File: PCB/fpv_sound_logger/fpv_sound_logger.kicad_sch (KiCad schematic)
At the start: 26 parts, among them IC1 W25Q128JVSIQ, IC2 NCP1117ST33T3G, J1 DM3D-SF, U1 RP2040, Y1 ABM8-272-T3

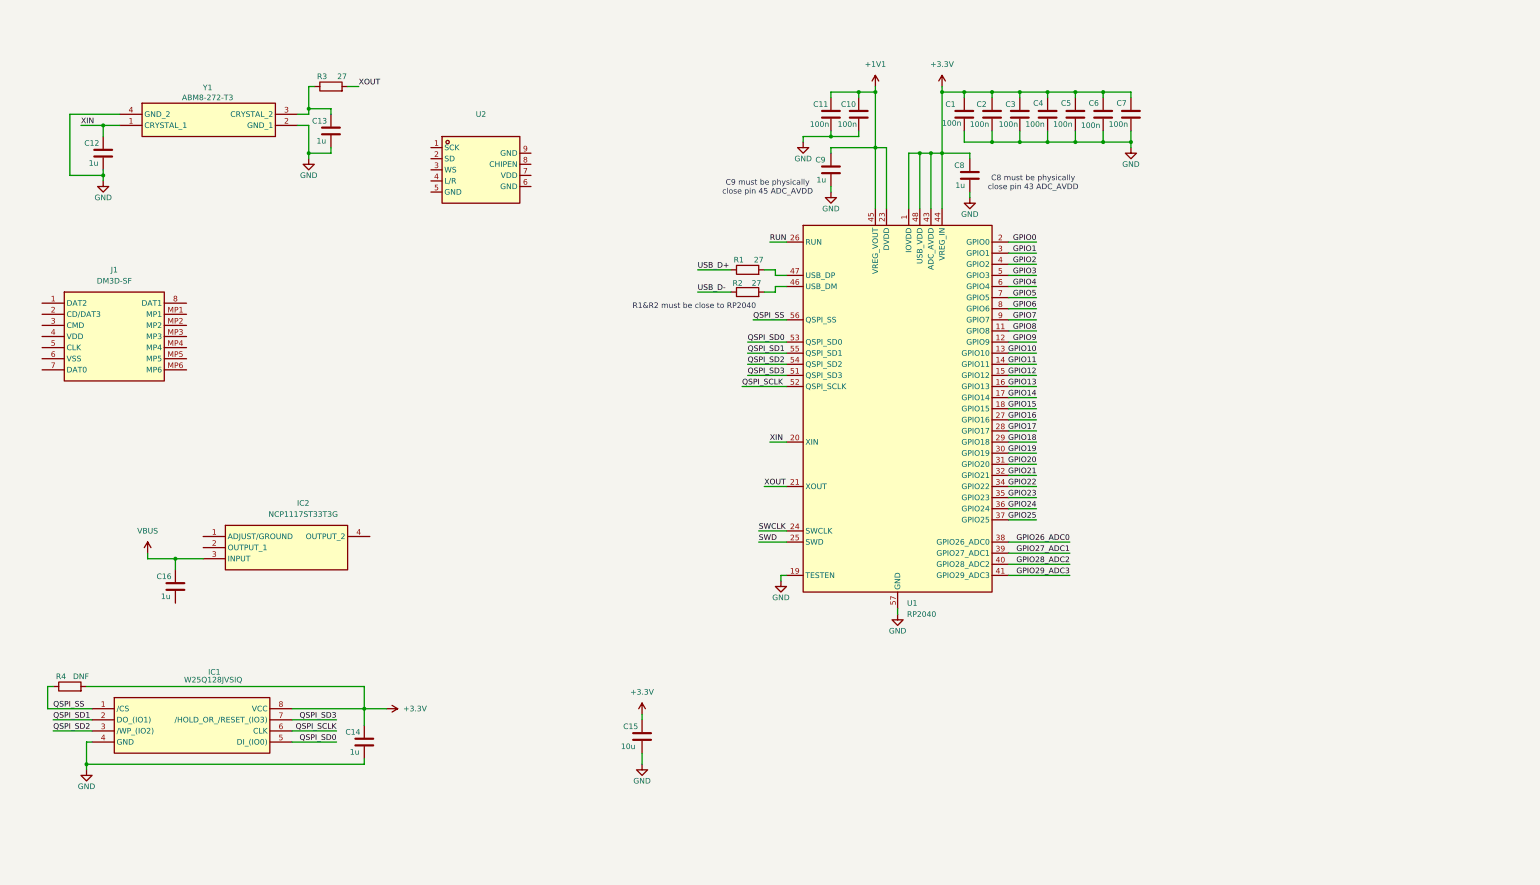
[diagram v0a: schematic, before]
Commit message: PCB: add every components, now designing according to datasheets
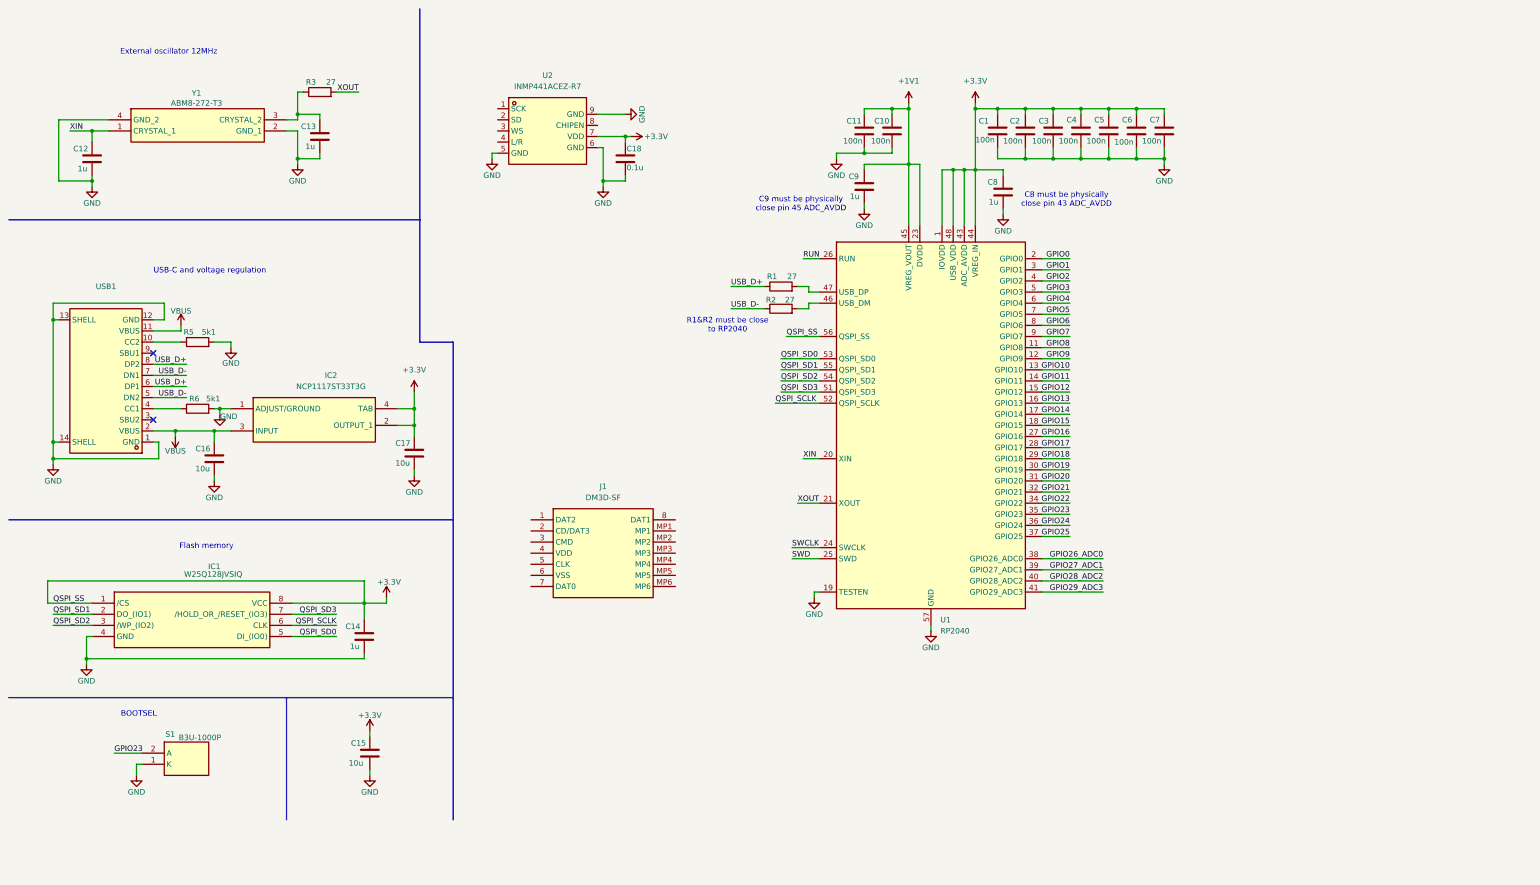
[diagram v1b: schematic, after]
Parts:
- removed R4: DNF, symbol Device:R
- added C17: 10u, symbol Device:C
- added C18: 0.1u, symbol Device:C
- added R5, R6: 5k1, symbol Device:R
- added S1: B3U-1000P, B3U-1000P, symbol SoundLogger:B3U-1000P
- added USB1: ~, fpv_sound_logger:USB-C-SMD_TYPE-C-6PIN-2MD-073, symbol SoundLogger:TYPE-C 16PIN 2MD(073)
- C16: value 1u -> 10u
- U2: value ~ -> INMP441ACEZ-R7
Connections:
- net QSPI_SS is gone; now on net +3.3V: IC1.1 (/CS), U1.56 (QSPI_SS)
- net +3.3V: now also IC2.2 (OUTPUT_1), IC2.4 (TAB), U2.7 (VDD), C17.1, C18.1
- net GND: now also C16.2, IC2.1 (ADJUST/GROUND), U2.5 (GND), U2.6 (GND), U2.9 (GND), C17.2, C18.2, R5.2, R6.2, S1.1 (K), USB1.1 (GND), USB1.12 (GND), USB1.13 (SHELL), USB1.14 (SHELL)
- net GPIO23: now also S1.2 (A)
- net USB_D+: now also USB1.6 (DP1), USB1.8 (DP2)
- net USB_D-: now also USB1.5 (DN2), USB1.7 (DN1)
- net VBUS: now also USB1.11 (VBUS), USB1.2 (VBUS)
- new net: R5.1, USB1.10 (CC2)
- new net: R6.1, USB1.4 (CC1)
- no-connect marks 0 -> 2
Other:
- note added: "BOOTSEL"
- note added: "External oscillator 12MHz"
- note added: "Flash memory"
- note added: "USB-C and voltage regulation"
- moved on the sheet: C1, C10, C11, C12, C13, C14, C15, C16, C2, C3, C4, C5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

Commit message: PCB: add JST connector, shottky diode, and few debugging
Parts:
- added C19: 100n, symbol Device:C
- added C20: 1u, symbol Device:C
- added CN1: SM04B-SRSS-TB(LF)(SN), fpv_sound_logger:CONN-SMD_4P-P1.00_SM04B-SRSS-TB-LF-SN, symbol SoundLogger:SM04B-SRSS-TB (LF)(SN)
- added D1, D2: SS14, fpv_sound_logger:DIOM5227X270N, symbol SoundLogger:SS14
- added R4: 47k, symbol Device:R
- added R7: 22, symbol Device:R
- added R8: 10k, symbol Device:R
- added TP1, TP2, TP3, TP4: TestPoint, TestPoint:TestPoint_Pad_D1.0mm, symbol Connector:TestPoint
- IC1: footprint SOIC127P790X216-8N -> fpv_sound_logger:SOIC127P790X216-8N
- IC2: footprint SOT230P700X180-4N -> fpv_sound_logger:SOT230P700X180-4N
- S1: footprint B3U-1000P -> fpv_sound_logger:B3U-1000P
- USB1: value ~ -> TYPE-C 16PIN 2MD(073)
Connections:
- net +3.3V: now also J1.4 (VDD), U2.8 (CHIPEN), C19.1, C20.1, R4.1, R8.1, TP4.1; no longer IC1.1 (/CS), U1.56 (QSPI_SS)
- net GND: now also J1.6 (VSS), J1.MP1, J1.MP2, J1.MP3, J1.MP4, J1.MP5, J1.MP6, U2.4 (L/R), C19.2, C20.2, CN1.3, CN1.5, CN1.6, TP3.1
- net GPIO1: now also CN1.2
- net GPIO10: now also R7.1
- net GPIO11: now also J1.3 (CMD)
- net GPIO12: now also J1.7 (DAT0)
- net GPIO13: now also J1.2 (CD/DAT3), R4.2
- net GPIO2: now also CN1.1
- net GPIO26_ADC0: now also U2.2 (SD)
- net GPIO27_ADC1: now also U2.1 (SCK)
- net GPIO28_ADC2: now also U2.3 (WS)
- net SWCLK: now also TP1.1
- net SWD: now also TP2.1
- net VBUS: now also D1.1 (K), D2.2 (A); no longer USB1.2 (VBUS)
- net at J1.5 (CLK): now also R7.2
- net GPIO0: no longer names the net of U1.2 (GPIO0)
- net GPIO14: no longer names the net of U1.17 (GPIO14)
- net GPIO15: no longer names the net of U1.18 (GPIO15)
- net GPIO16: no longer names the net of U1.27 (GPIO16)
- net GPIO17: no longer names the net of U1.28 (GPIO17)
- net GPIO18: no longer names the net of U1.29 (GPIO18)
- net GPIO19: no longer names the net of U1.30 (GPIO19)
- net GPIO20: no longer names the net of U1.31 (GPIO20)
- net GPIO21: no longer names the net of U1.32 (GPIO21)
- net GPIO22: no longer names the net of U1.34 (GPIO22)
- net GPIO24: no longer names the net of U1.36 (GPIO24)
- net GPIO25: no longer names the net of U1.37 (GPIO25)
- net GPIO29_ADC3: no longer names the net of U1.41 (GPIO29_ADC3)
- net GPIO3: no longer names the net of U1.5 (GPIO3)
- net GPIO4: no longer names the net of U1.6 (GPIO4)
- net GPIO5: no longer names the net of U1.7 (GPIO5)
- net GPIO6: no longer names the net of U1.8 (GPIO6)
- net GPIO7: no longer names the net of U1.9 (GPIO7)
- net GPIO8: no longer names the net of U1.11 (GPIO8)
- net GPIO9: no longer names the net of U1.12 (GPIO9)
- net RUN: no longer names the net of U1.26 (RUN)
- net RUN: now also R8.2
- new net: CN1.4, D1.2 (A)
- new net: D2.1 (K), USB1.2 (VBUS)
- new net QSPI_SS: IC1.1 (/CS), U1.56 (QSPI_SS)
- no-connect marks 2 -> 24
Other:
- note added: "JST 4-PIN connector"
- note added: "Microphone"
- note added: "SD connector"
- moved on the sheet: C16, C17, IC2, J1, R6

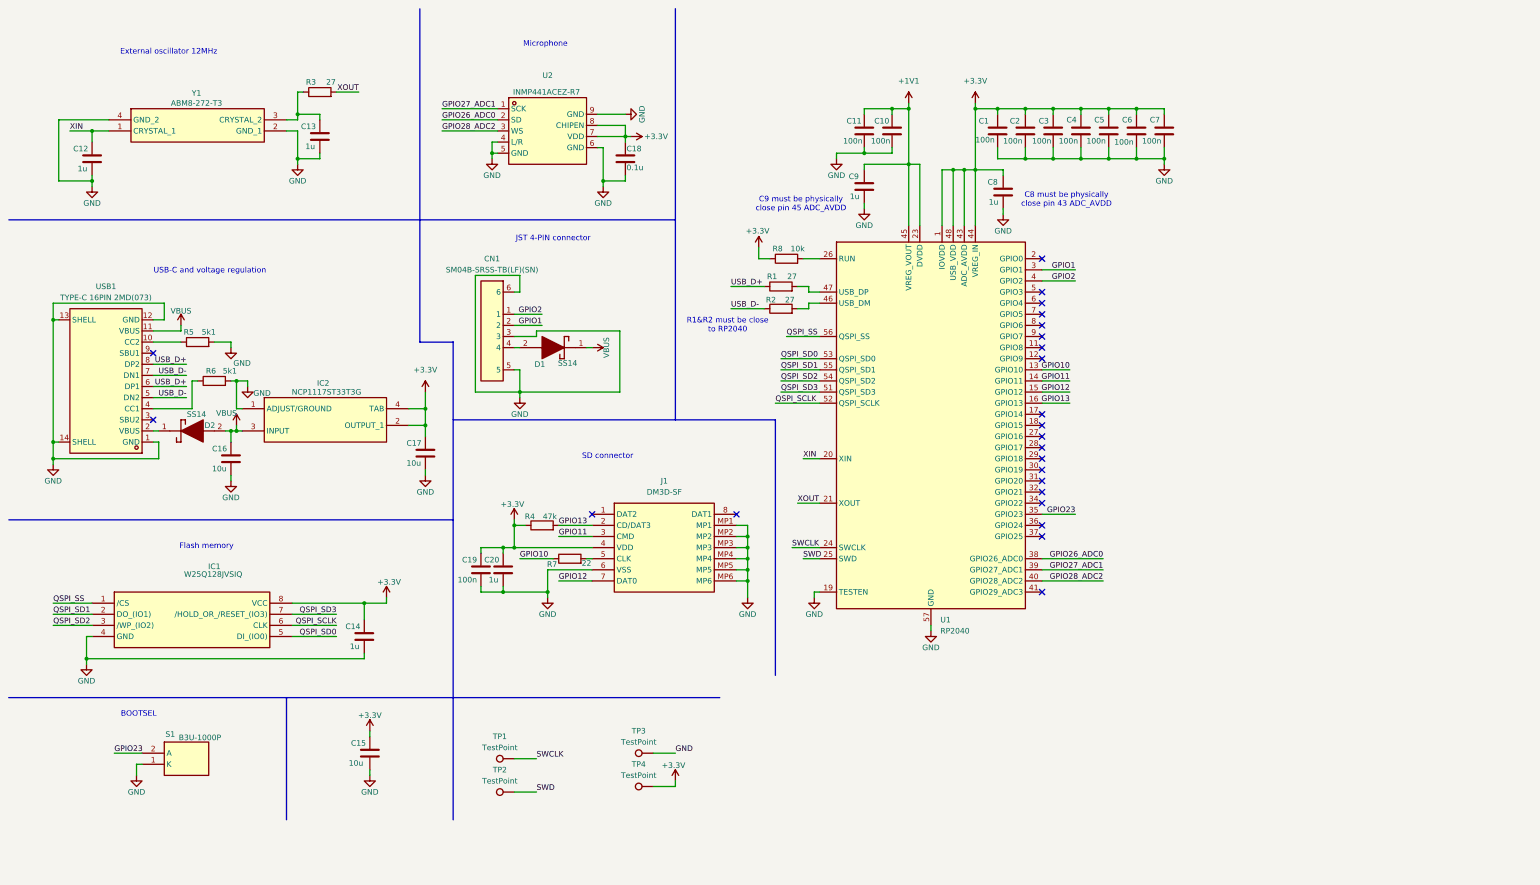
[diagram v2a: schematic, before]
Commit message: PCB: finished schematic, started placing components, not decided yet for board dimensions
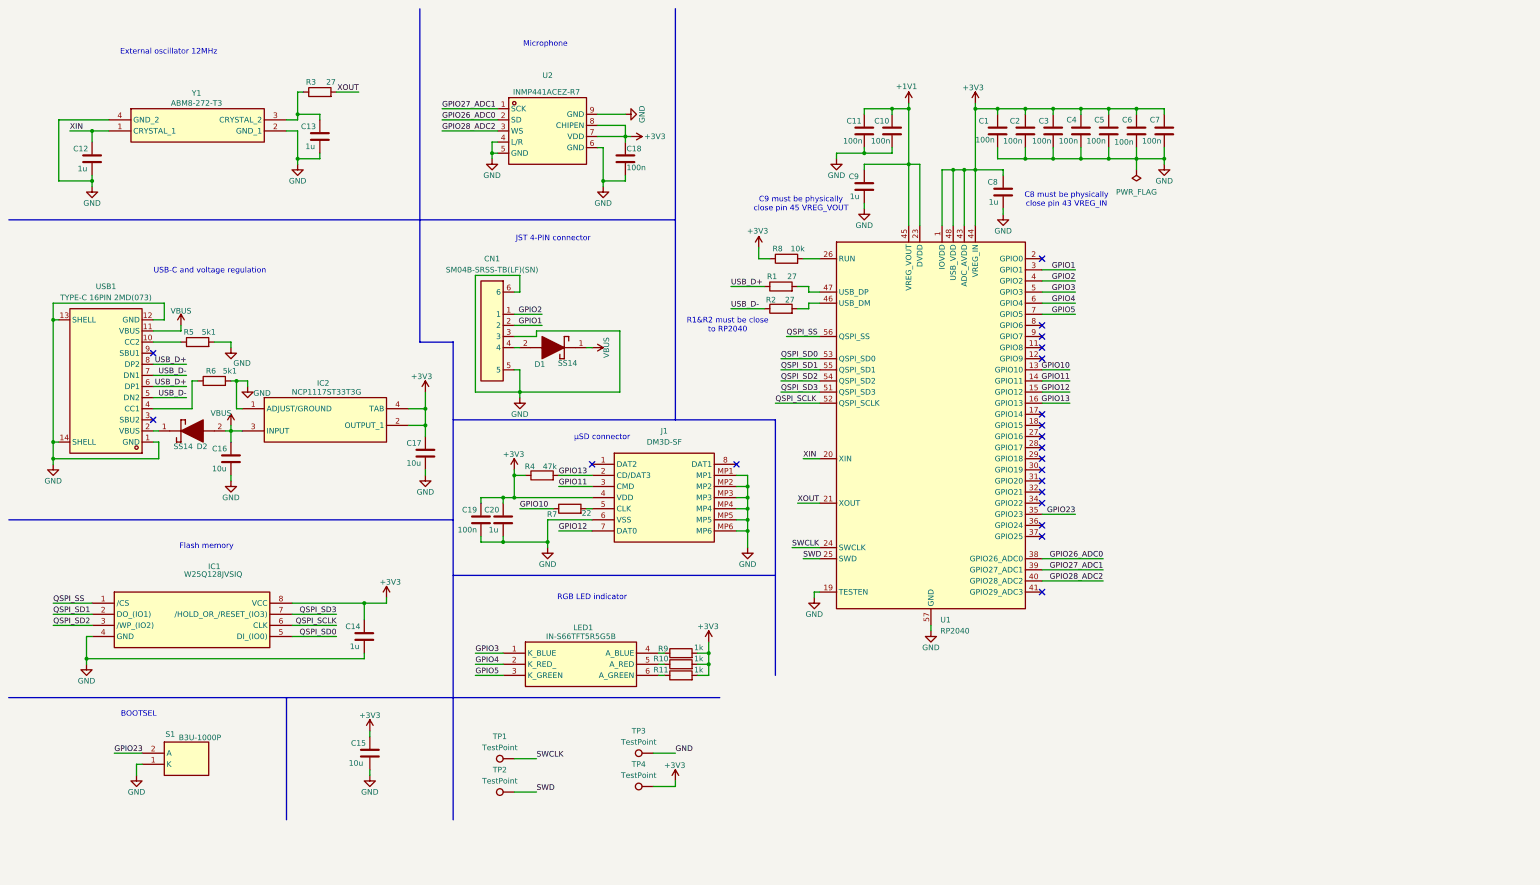
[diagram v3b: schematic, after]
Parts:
- added LED1: IN-S66TFT5R5G5B, fpv_sound_logger:INS66TFT5R5G5B, symbol SoundLogger:IN-S66TFT5R5G5B
- added R10, R11, R9: 1k, Resistor_SMD:R_0402_1005Metric, symbol Device:R
- C1, C10, C11, C19, C2, C3, C4, C5, C6, C7: footprint (none) -> Capacitor_SMD:C_0402_1005Metric; Manufacturer (none) -> YAGEO; Manufacturer_Part_Number (none) -> CC0402KRX7R7BB104
- C12, C13, C14, C20, C8, C9: footprint (none) -> Capacitor_SMD:C_0402_1005Metric; Manufacturer (none) -> YAGEO; Manufacturer_Part_Number (none) -> CC0402KRX5R6BB105
- C15, C16, C17: footprint (none) -> Capacitor_SMD:C_0402_1005Metric; Manufacturer (none) -> YAGEO; Manufacturer_Part_Number (none) -> CC0402MPX5R4BB106
- C18: value 0.1u -> 100n; footprint (none) -> Capacitor_SMD:C_0402_1005Metric; Manufacturer (none) -> YAGEO; Manufacturer_Part_Number (none) -> CC0402KRX7R7BB104
- CN1: Manufacturer_Part_Number (none) -> SM04B-SRSS-TB(LF)(SN)
- D1, D2, IC2: Manufacturer (none) -> onsemi
- IC1: Manufacturer (none) -> Winbond
- J1: Manufacturer (none) -> HRS
- R1, R2, R3: footprint (none) -> Resistor_SMD:R_0402_1005Metric; Manufacturer (none) -> YAGEO; Manufacturer_Part_Number (none) -> AC0402FR-0727RL
- R4: footprint (none) -> Resistor_SMD:R_0402_1005Metric; Manufacturer (none) -> YAGEO; Manufacturer_Part_Number (none) -> RC0402FR-7D47KL
- R5, R6: footprint (none) -> Resistor_SMD:R_0402_1005Metric; Manufacturer (none) -> YAGEO; Manufacturer_Part_Number (none) -> AC0402JR-075K1L
- R7: footprint (none) -> Resistor_SMD:R_0402_1005Metric; Manufacturer (none) -> YAGEO; Manufacturer_Part_Number (none) -> RC0402FR-7D22RL
- R8: footprint (none) -> Resistor_SMD:R_0402_1005Metric; Manufacturer (none) -> YAGEO; Manufacturer_Part_Number (none) -> AC0402FR-0710KL
- S1: Manufacturer (none) -> OMRON
- U1: Manufacturer (none) -> Raspberry Pi; Manufacturer_Part_Number (none) -> RP2040
- U2: Manufacturer (none) -> TDK InvenSense; Manufacturer_Part_Number (none) -> INMP441ACEZ-R7
- USB1: Manufacturer_Part_Number (none) -> TYPE-C 16PIN 2MD(073)
- Y1: Manufacturer (none) -> ABRACON
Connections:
- net GPIO3: now reaches U1.5 (GPIO3)
- net GPIO3: now also LED1.1 (K_BLUE)
- net GPIO4: now reaches U1.6 (GPIO4)
- net GPIO4: now also LED1.2 (K_RED_)
- net GPIO5: now reaches U1.7 (GPIO5)
- net GPIO5: now also LED1.3 (K_GREEN)
- net +3.3V renamed +3V3
- net +3V3: now also R10.2, R11.2, R9.2
- new net: LED1.4 (A_BLUE), R9.1
- new net: LED1.5 (A_RED), R10.1
- new net: LED1.6 (A_GREEN), R11.1
- no-connect marks 24 -> 21
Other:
- note added: "C8 must be physically close pin 43 VREG_IN"
- note added: "C9 must be physically close pin 45 VREG_VOUT"
- note added: "RGB LED indicator"
- note added: "µSD connector"
- note removed: "C8 must be physically close pin 43 ADC_AVDD"
- note removed: "C9 must be physically close pin 45 ADC_AVDD"
- note removed: "SD connector"
- moved on the sheet: C19, C20, J1, R4, R7

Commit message: PCB: started routing
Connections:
- net USB_DIFF-: now reaches R2.2, U1.46 (USB_DM)
- net USB_DIFF+: now reaches R1.2, U1.47 (USB_DP)
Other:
- moved on the sheet: R1, R2
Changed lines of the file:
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@@
 	(wire
 		(pts
-			(xy 193.04 76.2) (xy 195.58 76.2)
-		)
-		(stroke
-			(width 0)
-			(type default)
-		)
-	)
-	(wire
-		(pts
 			(xy 129.54 127) (xy 137.16 127)
 		)
@@
 	(wire
 		(pts
-			(xy 177.8 76.2) (xy 185.42 76.2)
+			(xy 170.18 76.2) (xy 177.8 76.2)
 		)
 		(stroke
@@
 	(wire
 		(pts
-			(xy 177.8 81.28) (xy 185.42 81.28)
+			(xy 170.18 81.28) (xy 177.8 81.28)
 		)
 		(stroke
@@
 	(wire
 		(pts
-			(xy 195.58 81.28) (xy 193.04 81.28)
+			(xy 240.03 58.42) (xy 240.03 59.69)
 		)
 		(stroke
@@
 	(wire
 		(pts
-			(xy 240.03 58.42) (xy 240.03 59.69)
+			(xy 248.92 95.25) (xy 255.27 95.25)
 		)
 		(stroke
@@
 	(wire
 		(pts
-			(xy 248.92 95.25) (xy 255.27 95.25)
+			(xy 195.58 77.47) (xy 198.12 77.47)
 		)
 		(stroke
@@
 	(wire
 		(pts
-			(xy 195.58 77.47) (xy 198.12 77.47)
+			(xy 63.5 88.9) (xy 59.69 88.9)
 		)
 		(stroke
@@
 	(wire
 		(pts
-			(xy 63.5 88.9) (xy 59.69 88.9)
+			(xy 63.5 119.38) (xy 63.5 120.65)
 		)
 		(stroke
@@
 	(wire
 		(pts
-			(xy 63.5 119.38) (xy 63.5 120.65)
+			(xy 251.46 35.56) (xy 251.46 36.83)
 		)
 		(stroke
@@
 	(wire
 		(pts
-			(xy 251.46 35.56) (xy 251.46 36.83)
+			(xy 148.59 44.45) (xy 148.59 52.07)
 		)
 		(stroke
@@
 	(wire
 		(pts
-			(xy 148.59 44.45) (xy 148.59 52.07)
+			(xy 185.42 81.28) (xy 195.58 81.28)
 		)
 		(stroke
@@
 	(wire
 		(pts
+			(xy 185.42 76.2) (xy 195.58 76.2)
+		)
+		(stroke
+			(width 0)
+			(type default)
+		)
+	)
+	(wire
+		(pts
 			(xy 128.27 82.55) (xy 134.62 82.55)
 		)
@@
 	)
 	(label "USB_D+"
-		(at 177.8 76.2 0)
+		(at 170.18 76.2 0)
 		(effects
 			(font
@@
 	)
 	(label "USB_D-"
-		(at 177.8 81.28 0)
+		(at 170.18 81.28 0)
 		(effects
 			(font
@@
 		)
 	)
+	(label "USB_DIFF-"
+		(at 186.69 81.28 0)
+		(effects
+			(font
+				(size 1.27 1.27)
+			)
+			(justify left bottom)
+		)
+	)
 	(label "QSPI_SD2"
 		(at 22.86 153.67 0)
@@
 		)
 	)
+	(label "USB_DIFF+"
+		(at 186.69 76.2 0)
+		(effects
+			(font
+				(size 1.27 1.27)
+			)
+			(justify left bottom)
+		)
+	)
 	(label "USB_D-"
 		(at 53.34 96.52 180)
@@
 	(symbol
 		(lib_id "Device:R")
-		(at 189.23 81.28 90)
+		(at 181.61 81.28 90)
 		(unit 1)
 		(exclude_from_sim no)
@@
 		(dnp no)
 		(property "Reference" "R2"
-			(at 186.944 79.248 90)
+			(at 179.324 79.248 90)
 			(effects
 				(font
@@
 		)
 		(property "Value" "27"
-			(at 191.262 79.248 90)
+			(at 183.642 79.248 90)
 			(effects
 				(font
@@
 		)
 		(property "Footprint" "Resistor_SMD:R_0402_1005Metric"
-			(at 189.23 83.058 90)
+			(at 181.61 83.058 90)
 			(effects
 				(font
@@
 		)
 		(property "Datasheet" "~"
-			(at 189.23 81.28 0)
+			(at 181.61 81.28 0)
 			(effects
 				(font
@@
 		)
 		(property "Description" "Resistor"
-			(at 189.23 81.28 0)
+			(at 181.61 81.28 0)
 			(effects
 				(font
@@
 		)
 		(property "Manufacturer" "YAGEO"
-			(at 189.23 81.28 90)
+			(at 181.61 81.28 90)
 			(effects
 				(font
@@
 		)
 		(property "Manufacturer_Part_Number" "AC0402FR-0727RL"
-			(at 189.23 81.28 90)
+			(at 181.61 81.28 90)
 			(effects
 				(font
@@
 	(symbol
 		(lib_id "Device:R")
-		(at 189.23 76.2 90)
+		(at 181.61 76.2 90)
 		(unit 1)
 		(exclude_from_sim no)
@@
 		(dnp no)
 		(property "Reference" "R1"
-			(at 187.198 73.914 90)
+			(at 179.578 73.914 90)
 			(effects
 				(font
@@
 		)
 		(property "Value" "27"
-			(at 191.77 73.914 90)
+			(at 184.15 73.914 90)
 			(effects
 				(font
@@
 		)
 		(property "Footprint" "Resistor_SMD:R_0402_1005Metric"
-			(at 189.23 77.978 90)
+			(at 181.61 77.978 90)
 			(effects
 				(font
@@
 		)
 		(property "Datasheet" "~"
-			(at 189.23 76.2 0)
+			(at 181.61 76.2 0)
 			(effects
 				(font
@@
 		)
 		(property "Description" "Resistor"
-			(at 189.23 76.2 0)
+			(at 181.61 76.2 0)
 			(effects
 				(font
@@
 		)
 		(property "Manufacturer" "YAGEO"
-			(at 189.23 76.2 90)
+			(at 181.61 76.2 90)
 			(effects
 				(font
@@
 		)
 		(property "Manufacturer_Part_Number" "AC0402FR-0727RL"
-			(at 189.23 76.2 90)
+			(at 181.61 76.2 90)
 			(effects
 				(font
